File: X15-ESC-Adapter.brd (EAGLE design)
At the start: 101.6 x 41.1 mm, 10 parts, among them J1 IPBT-103-H1-T-S, J2 IPBT-103-H1-T-S, J3 IPBT-103-H1-T-S, J4 IPBT-103-H1-T-S

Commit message: Fix wire stubs to polygons
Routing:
- net ESC1_B: track 20.1 -> 0.00 mm
- net ESC3_B: track 17.6 -> 0.00 mm
- net ESC2_B: track 16.2 -> 0.00 mm
- net ESC1_Y: track 12.8 -> 0.00 mm
- net ESC1_R: track 12.5 -> 0.00 mm
- net ESC4_B: track 11.3 -> 0.00 mm
- net ESC4_Y: track 11.1 -> 0.00 mm
- net ESC2_Y: track 11.1 -> 0.00 mm
- net ESC2_R: track 10.6 -> 0.00 mm
- net ESC3_Y: track 10.4 -> 0.00 mm
- net ESC3_R: track 10.2 -> 0.00 mm
- net ESC4_R: track 7.40 -> 0.00 mm

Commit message: Adjusted the IPBT Footprint
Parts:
- J1, J2, J3, J4: value IPBT-103-H1-T-S -> IBPT-103-H1-T-S-RA; device X15-ESC-Adapter:IPBT-103-H1-T-S -> X15-ESC-Adapter:IPBT-103-H1-T-S-RA
- moved J4 3.89 mm to (91.5, 6.96)
- moved J2 3.78 mm to (10.2, 6.99)
- moved J1 3.71 mm to (10.2, 27.6)
- moved J3 3.68 mm to (91.3, 27.5)
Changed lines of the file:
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@@
 <attribute name="VALUE" x="98.298" y="14.986" size="0.6096" layer="27" font="vector" ratio="20" align="top-center"/>
 </element>
-<element name="J1" library="X15-ESC-Adapter" package="IPBT-103-H1-T-S" package3d_urn="urn:adsk.eagle:package:37886187/2" value="IPBT-103-H1-T-S" x="13.9192" y="27.6098" smashed="yes" rot="R90"/>
-<element name="J2" library="X15-ESC-Adapter" package="IPBT-103-H1-T-S" package3d_urn="urn:adsk.eagle:package:37886187/2" value="IPBT-103-H1-T-S" x="13.97" y="6.985" smashed="yes" rot="R90"/>
-<element name="J3" library="X15-ESC-Adapter" package="IPBT-103-H1-T-S" package3d_urn="urn:adsk.eagle:package:37886187/2" value="IPBT-103-H1-T-S" x="87.63" y="27.6352" smashed="yes" rot="R270"/>
-<element name="J4" library="X15-ESC-Adapter" package="IPBT-103-H1-T-S" package3d_urn="urn:adsk.eagle:package:37886187/2" value="IPBT-103-H1-T-S" x="87.6554" y="6.985" smashed="yes" rot="R270"/>
+<element name="J1" library="X15-ESC-Adapter" package="IPBT-103-H1-T-S-RA" package3d_urn="urn:adsk.eagle:package:38819791/3" value="IBPT-103-H1-T-S-RA" x="10.2108" y="27.559" smashed="yes" rot="R90"/>
+<element name="J2" library="X15-ESC-Adapter" package="IPBT-103-H1-T-S-RA" package3d_urn="urn:adsk.eagle:package:38819791/3" value="IBPT-103-H1-T-S-RA" x="10.1854" y="6.985" smashed="yes" rot="R90"/>
+<element name="J3" library="X15-ESC-Adapter" package="IPBT-103-H1-T-S-RA" package3d_urn="urn:adsk.eagle:package:38819791/3" value="IBPT-103-H1-T-S-RA" x="91.313" y="27.5336" smashed="yes" rot="R270"/>
+<element name="J4" library="X15-ESC-Adapter" package="IPBT-103-H1-T-S-RA" package3d_urn="urn:adsk.eagle:package:38819791/3" value="IBPT-103-H1-T-S-RA" x="91.5416" y="6.9596" smashed="yes" rot="R270"/>
 <element name="LUMENIER_ESC" library="X15-ESC-Adapter" package="LUMENIER" package3d_urn="urn:adsk.eagle:package:37886188/1" value="LUMENIER" x="27.813" y="0.508" smashed="yes"/>
 </elements>

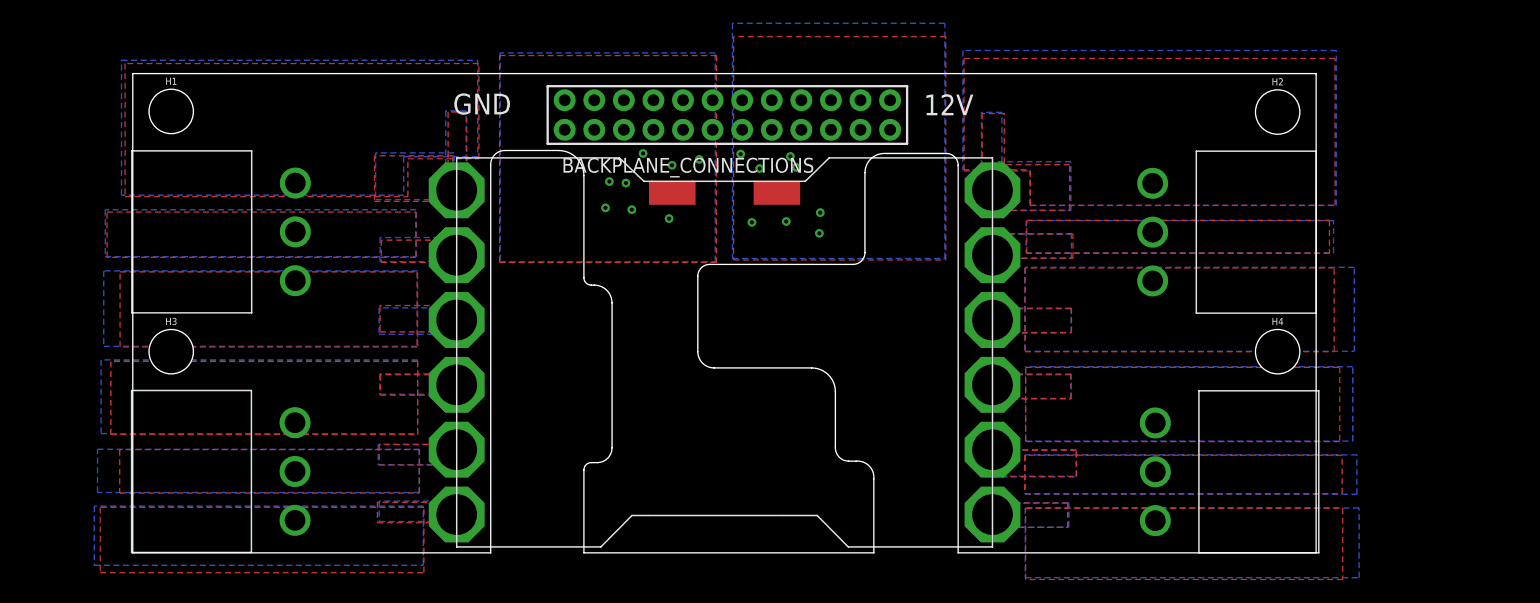
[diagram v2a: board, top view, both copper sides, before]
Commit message: Complete ESC Adapter Design
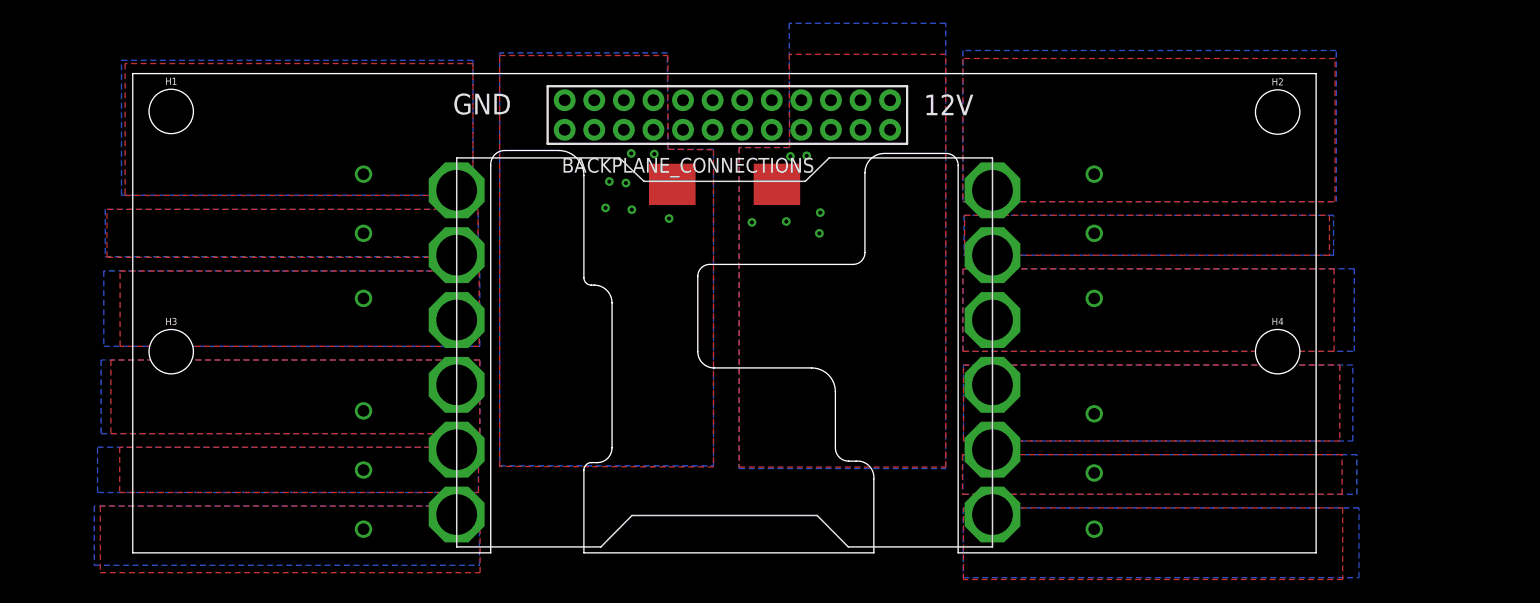
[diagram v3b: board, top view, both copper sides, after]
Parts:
- removed J1, J2, J3, J4: IBPT-103-H1-T-S-RA, X15-ESC-Adapter:IPBT-103-H1-T-S-RA
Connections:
- net 12V: no longer BACKPLANE_CONNECTIONS.12V@10, BACKPLANE_CONNECTIONS.12V@11, BACKPLANE_CONNECTIONS.12V@12, BACKPLANE_CONNECTIONS.12V@9
- net ESC1_B: no longer J1.3
- net ESC1_R: no longer J1.1
- net ESC1_Y: no longer J1.2
- net ESC2_B: no longer J2.3
- net ESC2_R: no longer J2.1
- net ESC2_Y: no longer J2.2
- net ESC3_B: no longer J3.1
- net ESC3_R: no longer J3.3
- net ESC3_Y: no longer J3.2
- net ESC4_B: no longer J4.1
- net ESC4_R: no longer J4.3
- net ESC4_Y: no longer J4.2
- net GND: no longer BACKPLANE_CONNECTIONS.GND@1, BACKPLANE_CONNECTIONS.GND@2, BACKPLANE_CONNECTIONS.GND@3, BACKPLANE_CONNECTIONS.GND@4

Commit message: Update to v2
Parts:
- removed H3, H4: 6-32-HOLE, X15-ESC-Adapter:6-32-HOLE
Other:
- outline, holes or cut-outs redrawn
- board text added: "X15 ESC Adapter v2 Derek Chi Bryce Sasser Minh Nguyen"
